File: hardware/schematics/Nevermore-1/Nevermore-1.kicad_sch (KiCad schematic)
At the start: 2 parts, among them U1 XIAO-ESP32-S3-SMD, U2 MPU-6050

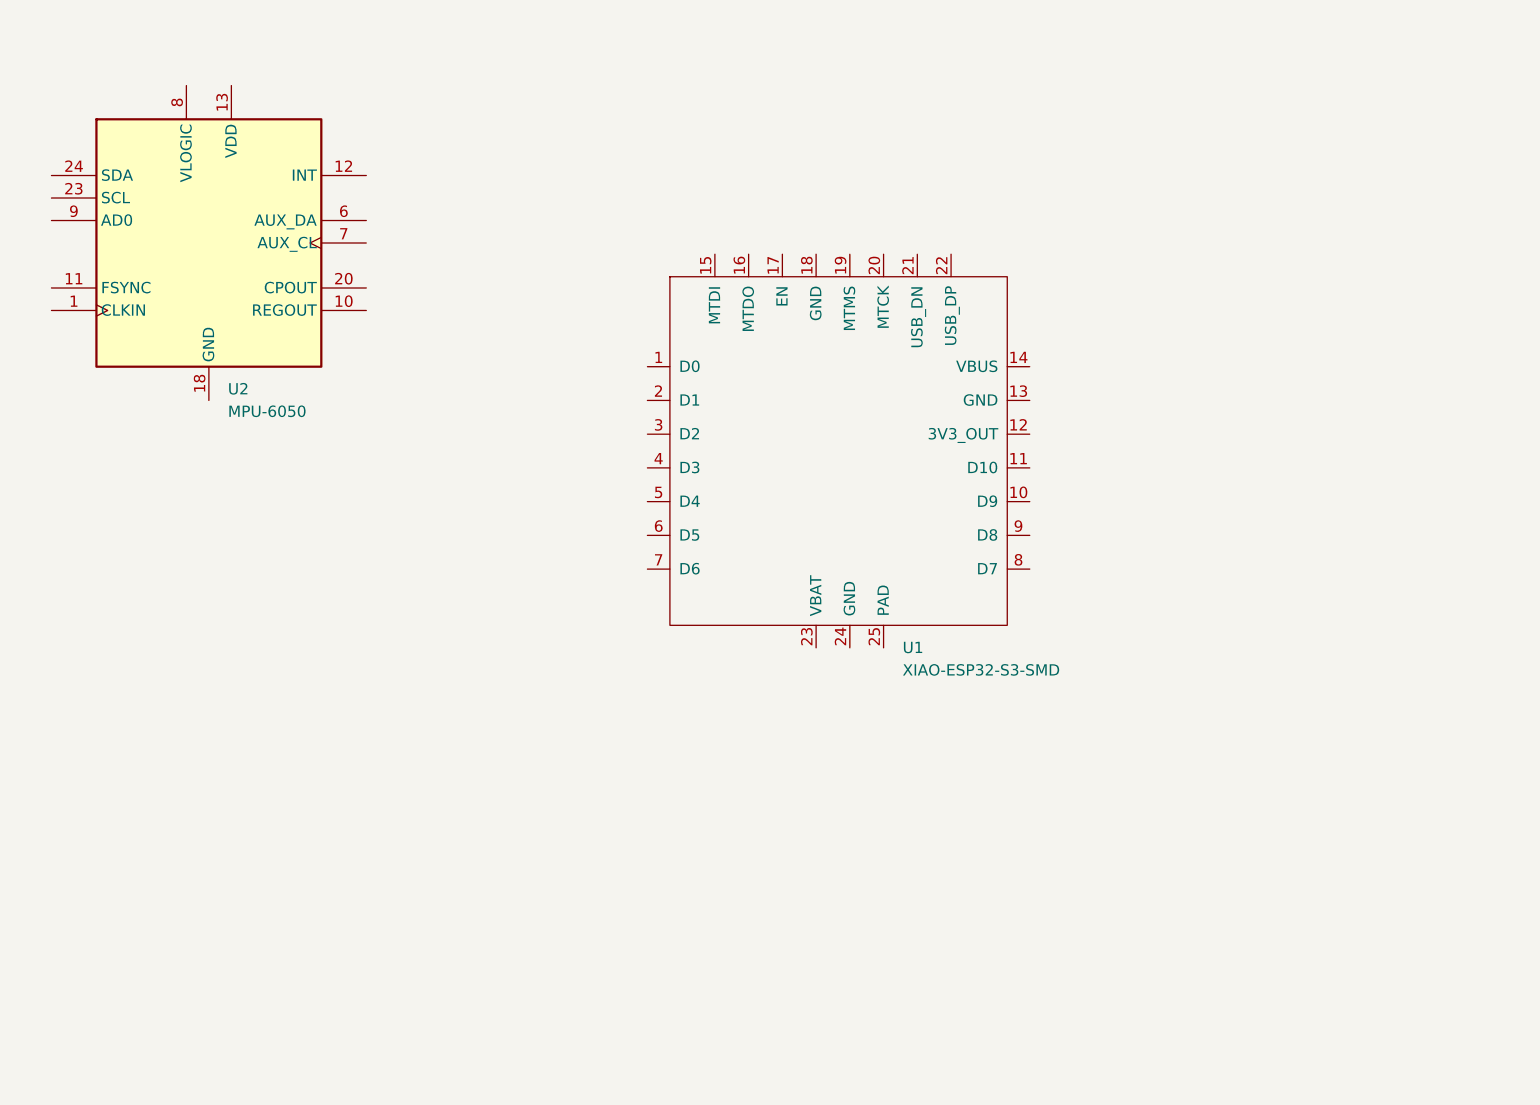
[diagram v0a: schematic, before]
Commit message: Enhance sensor configuration and calculations in main application; update gyro and accel ranges, improve pitch and roll calculations
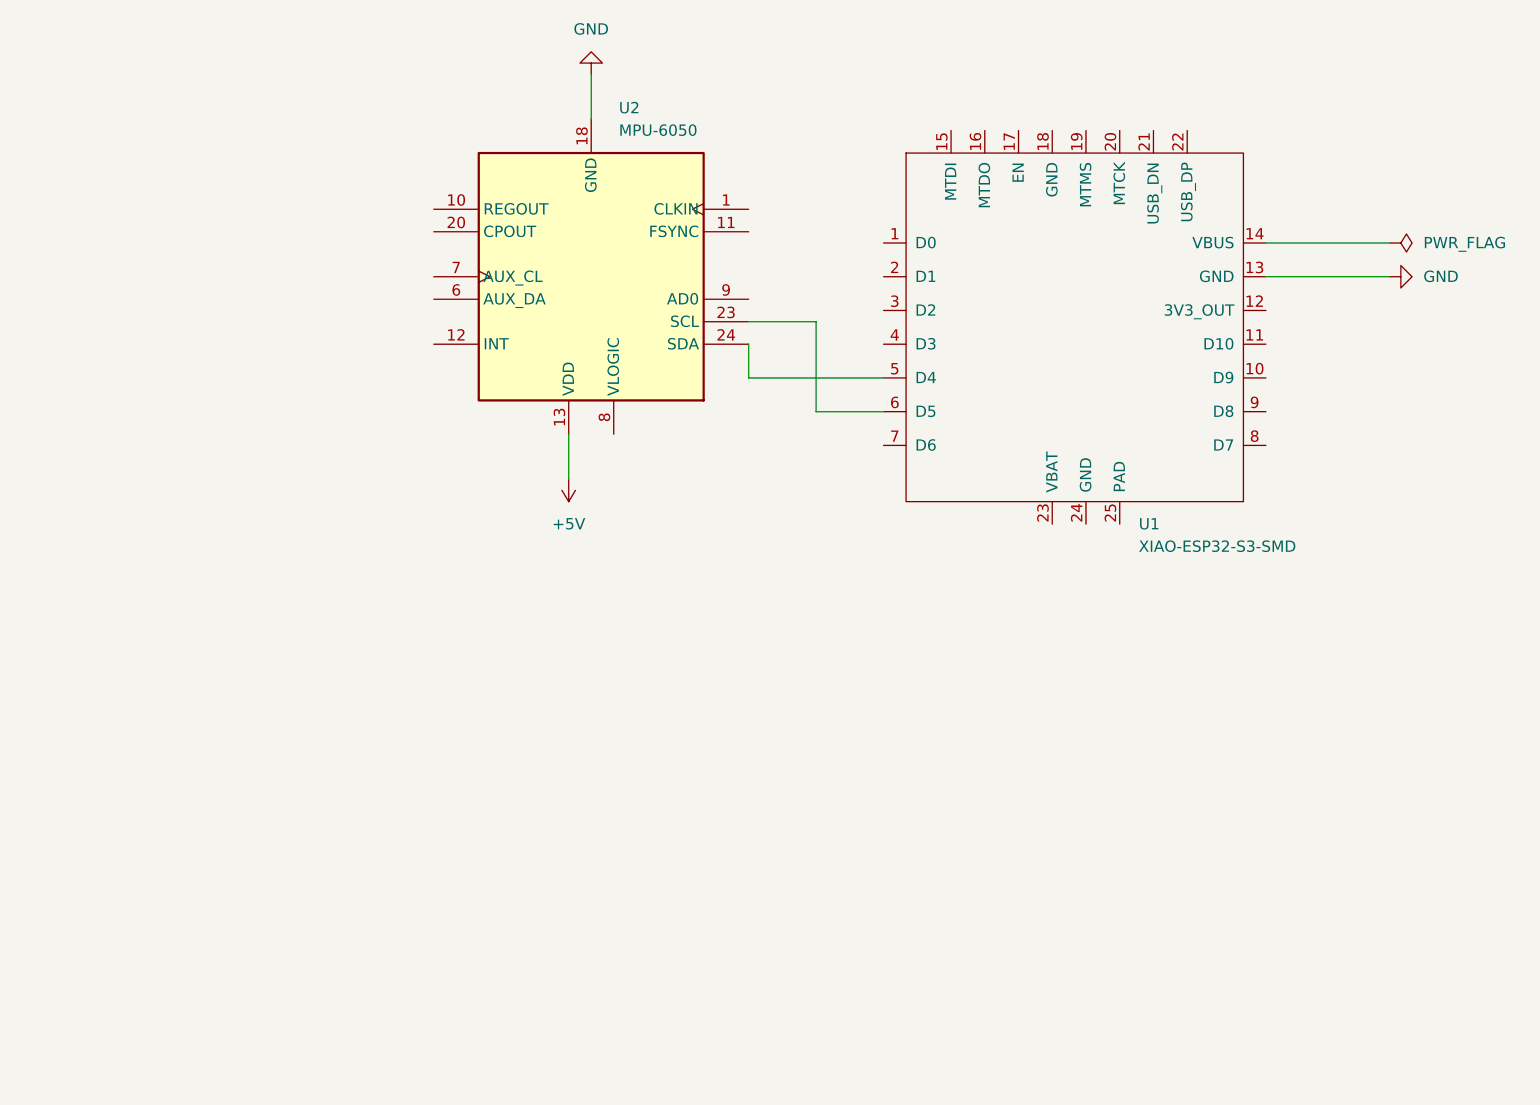
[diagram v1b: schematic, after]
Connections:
- net +5V: now reaches U2.13 (VDD)
- net GND: now reaches U2.18 (GND)
- net GND: now also U1.13 (GND)
- net at U2.23 (SCL): now also U1.6 (D5)
- net at U2.24 (SDA): now also U1.5 (D4)
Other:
- moved on the sheet: U1, U2

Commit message: Remove lock files for Nevermore-1 schematics to clean up project directory
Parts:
- added J1: MODULO_GPS_NEO6M, symbol Connector_Generic:Conn_01x04
- added M1, M2, M3: Motor_Servo, symbol Motor:Motor_Servo
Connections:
- net +5V: now also J1.1 (Pin_1), M1.2 (+), M2.2 (+), M3.2 (+)
- net GND: now also J1.2 (Pin_2), M1.3 (-), M2.3 (-), M3.3 (-)
- net I2C_SCL: now reaches U1.6 (D5), U2.23 (SCL)
- net I2C_SDA: now reaches U1.5 (D4), U2.24 (SDA)
- net SERVO_PITCH1: now reaches U1.1 (D0)
- net SERVO_PITCH1: now also M3.1 (PWM)
- net SERVO_PITCH2: now reaches U1.2 (D1)
- net SERVO_PITCH2: now also M2.1 (PWM)
- net SERVO_PITCH3: now reaches U1.3 (D2)
- net SERVO_PITCH3: now also M1.1 (PWM)
- net GPS_RX: now reaches U1.7 (D6)
- net GPS_RX: now also J1.4 (Pin_4)
- net GPS_TX: now reaches U1.8 (D7)
- net GPS_TX: now also J1.3 (Pin_3)
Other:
- moved on the sheet: U1, U2
